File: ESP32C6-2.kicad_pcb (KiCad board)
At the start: 2 copper layers, 41.1 x 32 mm, 21 parts, among them J1 DE9_Pins, J2 Screw_Terminal_01x04, U1 XIAO-ESP32-C6/SUPERMini, U2 SN65HVD230DR, U3 LMR51430YDDCR

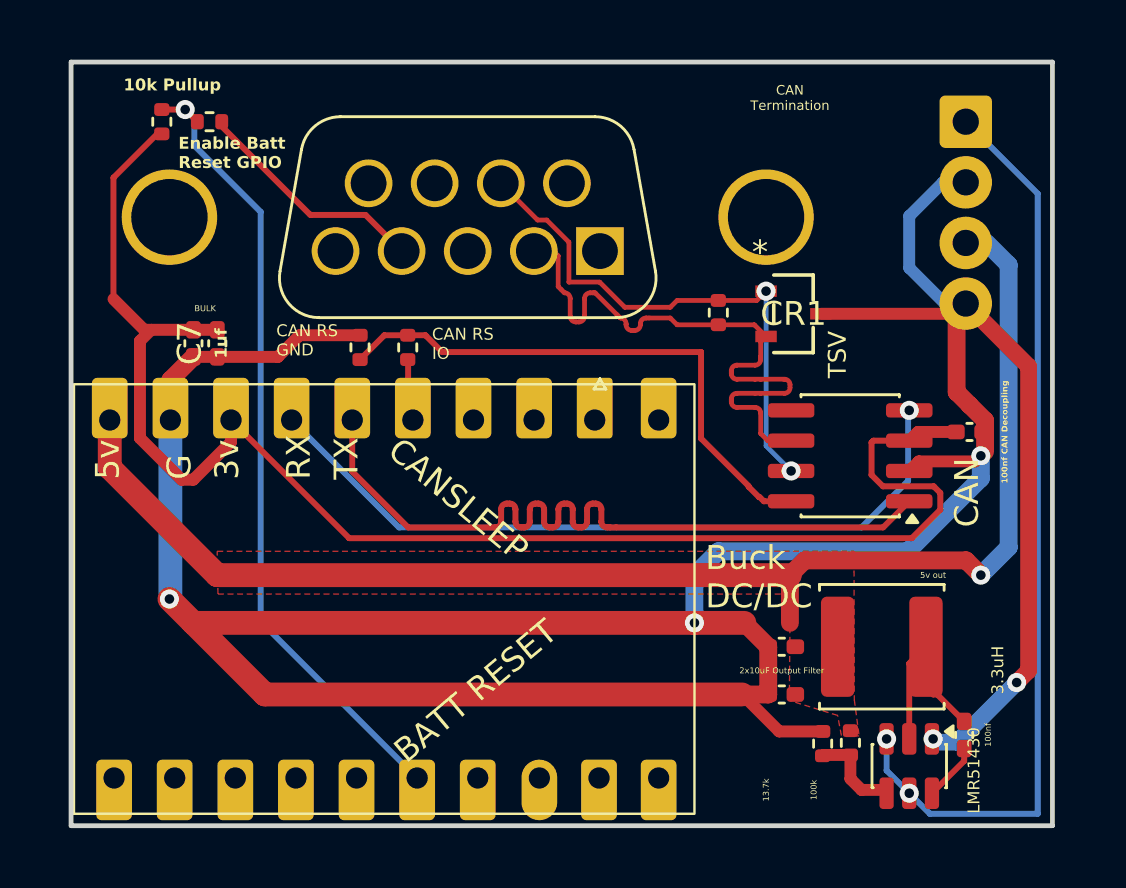
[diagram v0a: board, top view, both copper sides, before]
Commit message: Update to add TVS and ground plane
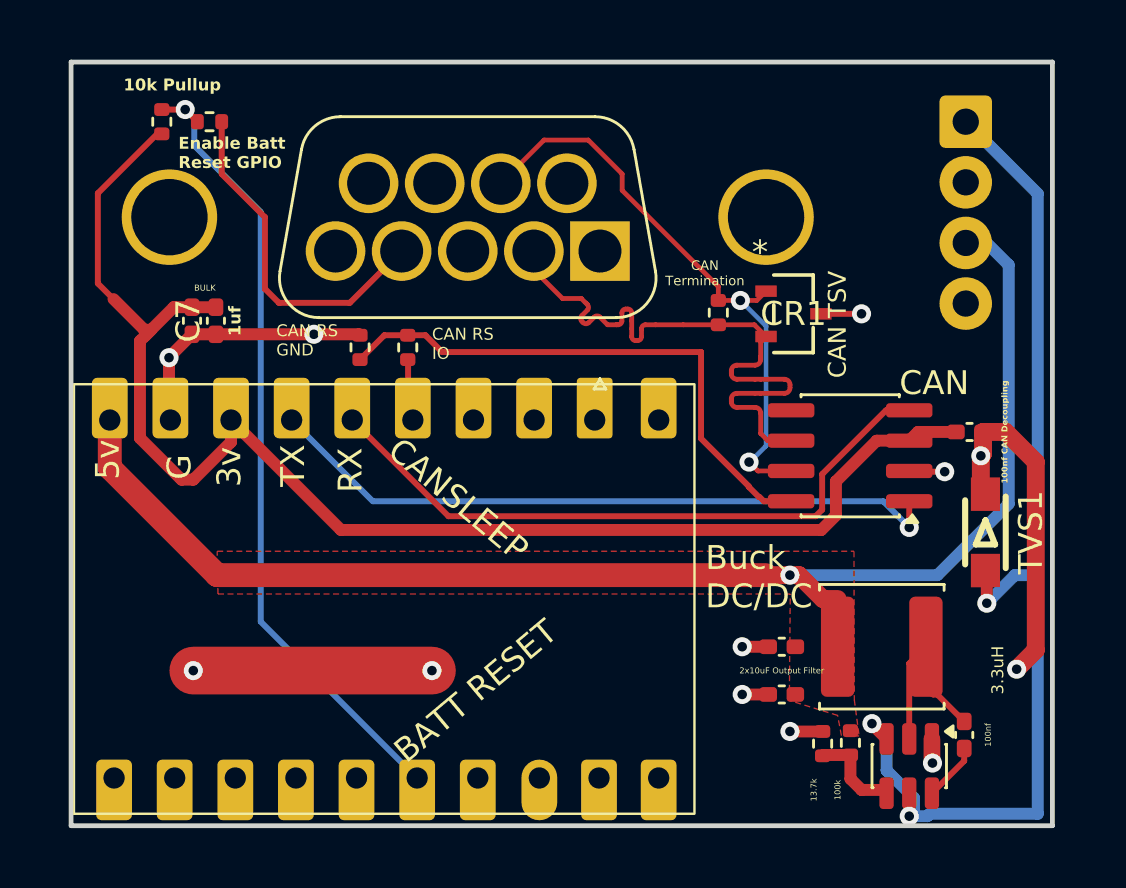
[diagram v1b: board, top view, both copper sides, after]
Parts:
- added TVS1: 24v TVS C918843, JPGIndustriesCustom:TVS SOD-123FL_L3.0-W1.8-LS3.7-RD C918843, F.Cu at (150.2, 65.2)
- C3, C5: value 10uf -> 10uf C15525
- C7: value 1uf -> 1uf C52923
- CR1: value PESD1CAN_215 -> PESD1CAN_215 C284094
- R1, R2, R5: value 0R -> 0R C17168
- R3: value 120R -> 120R C25079
- R6: value 10K -> 10K C25744
- R7: value 100K -> 100K C25741
- R8: value 13.7K -> 13.7K C25854
- moved C4 0.95 mm to (116.9, 56.3)
- moved C7 0.95 mm to (117.9, 56.3)
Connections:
- U2 pad 1: Net-(U1-GPIO19) -> Net-(U1-GPIO20)
- U2 pad 4: Net-(U1-GPIO20) -> Net-(U1-GPIO19)
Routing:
- net GND: track 139.3 -> 44.1 mm, vias 5 -> 12
- net Net-(J2-Pin_1): track 38.7 -> 46.2 mm, vias 2 -> 3
- net Net-(U1-GPIO19): track 33.1 -> 27.7 mm
- net Net-(U1-3v3): track 64.8 -> 59.7 mm
- net Net-(J1-Pad4): track 9.90 -> 14.6 mm
- net Net-(U1-GPIO20): track 31.5 -> 28.8 mm
- net /CAN +: track 23.2 -> 25.0 mm
- net Net-(J2-Pin_3): track 58.5 -> 57.4 mm
- added copper zone on B.Cu, net GND
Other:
- board text added: "CAN TSV"
- board text removed: "5v out"
- board text removed: "LMR51430"
- board text removed: "TSV"

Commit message: Rev 1, as built
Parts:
- C6: value 100nf -> 100nf C307331
- U2: value SN65HVD230DR -> SN65HVD230DR C12084
- moved CR1 0.88 mm to (142.7, 56.7)
- moved R8 0.54 mm to (142.8, 74.0)
- moved R7 0.53 mm to (144.0, 74.0)
- moved R1 0.13 mm to (126.1, 57.5), turned to 0 degrees
- moved R2 0.12 mm to (123.9, 57.6), turned to 180 degrees
- turned TVS1 to 90 degrees
- renumbered U3 to U3C5210749
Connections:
- net Net-(J2-Pin_3) renamed +5V
- TVS1 pad 1: GND -> Net-(J2-Pin_1)
- TVS1 pad 2: Net-(J2-Pin_1) -> GND
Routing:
- net GND: track 44.1 -> 16.1 mm, vias 12 -> 14
- net Net-(J2-Pin_1): track 46.2 -> 45.2 mm
- net /CAN -: track 26.9 -> 27.7 mm
- net Net-(U1-GPIO18): track 2.68 -> 3.40 mm
- net /CAN +: track 25.0 -> 25.6 mm
- added copper zone on F.Cu, net GND
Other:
- board size 41.1 x 32 mm -> 43 x 33 mm
- board text added: "CAN TVS"
- board text removed: "CAN TSV"
